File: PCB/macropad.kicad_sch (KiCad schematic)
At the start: 39 parts, among them SW1 SW_Push, SW10 SW_Push, SW11 SW_Push, SW12 SW_Push, SW13 SW_Push, SW14 SW_Push, SW15 SW_Push, SW16 SW_Push, SW2 SW_Push, SW3 SW_Push, SW4 SW_Push, SW5 SW_Push, SW6 SW_Push, SW7 SW_Push, SW8 SW_Push, SW9 SW_Push, U2 MOUDLE-SEEEDUINO-XIAO

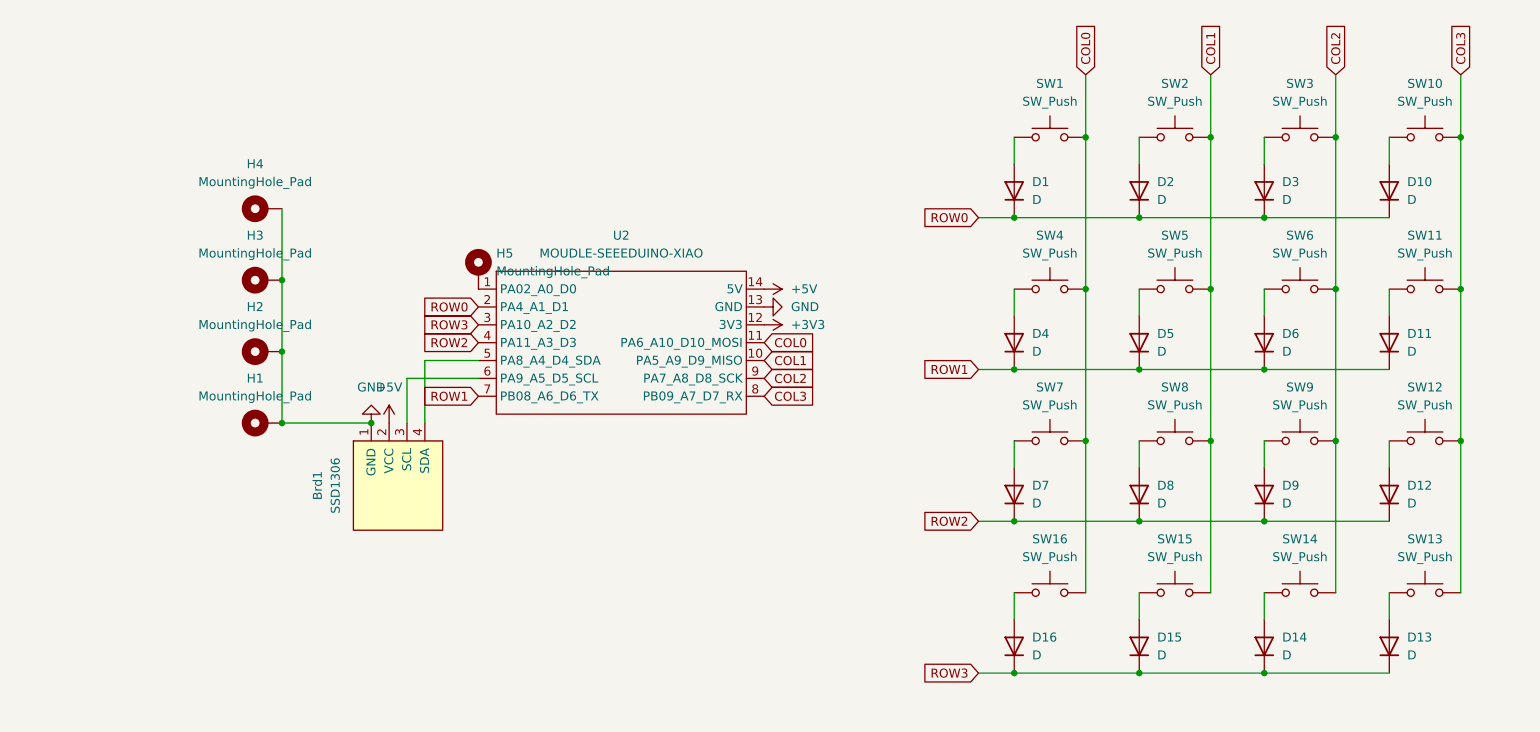
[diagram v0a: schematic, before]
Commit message: Add pullup resistors for I2C
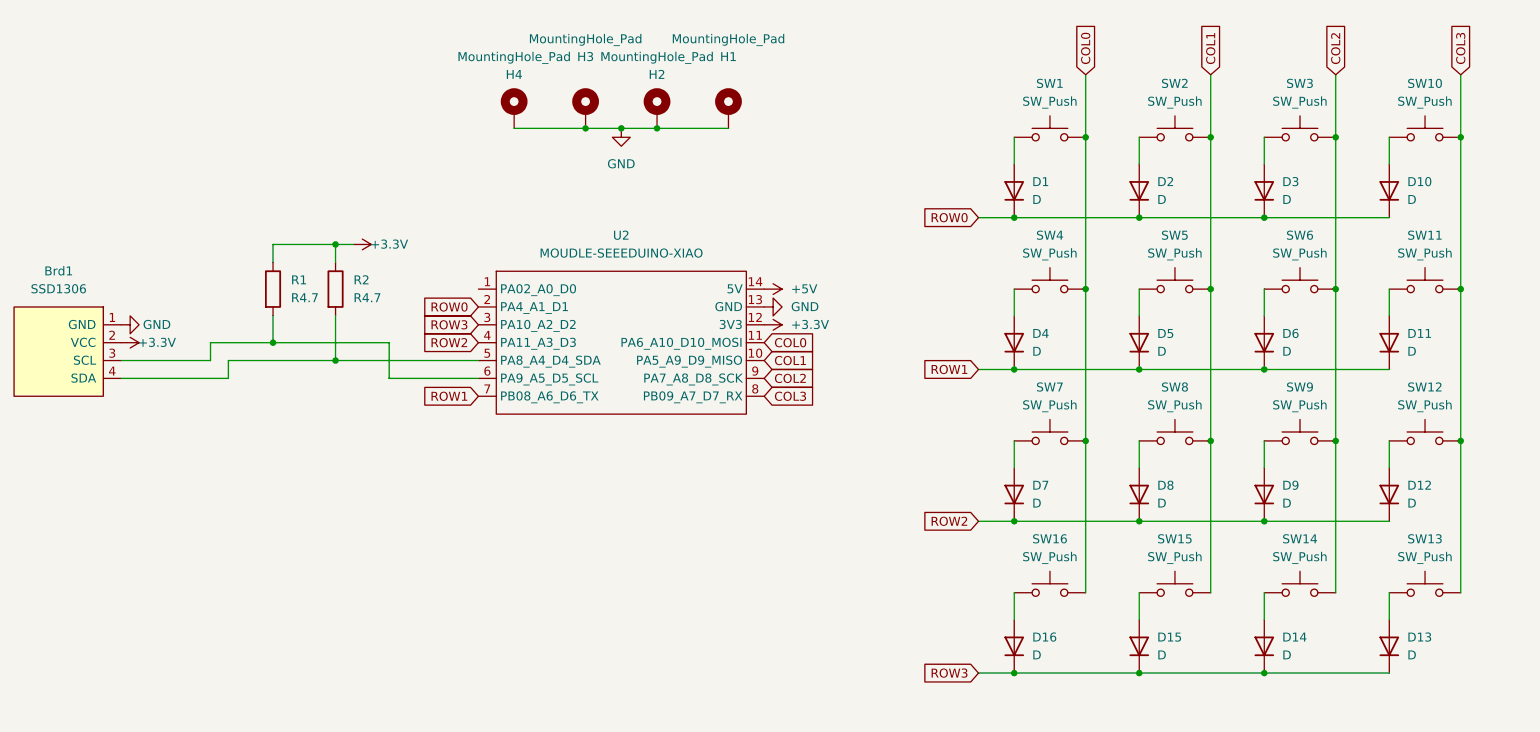
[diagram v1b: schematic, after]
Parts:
- removed H5: MountingHole_Pad, Connector_Wire:SolderWire-0.1sqmm_1x01_D0.4mm_OD1mm, symbol Mechanical:MountingHole_Pad
- added R1, R2: R4.7, Resistor_THT:R_Axial_DIN0204_L3.6mm_D1.6mm_P7.62mm_Horizontal, symbol Device:R
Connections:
- net +5V: no longer Brd1.2 (VCC)
- net at Brd1.4 (SDA), U2.5 (PA8_A4_D4_SDA): now also R2.2
- net at Brd1.3 (SCL), U2.6 (PA9_A5_D5_SCL): now also R1.2
- net +3V3 renamed +3.3V
- net +3.3V: now also Brd1.2 (VCC), R1.1, R2.1
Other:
- moved on the sheet: Brd1, H1, H2, H3, H4

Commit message: Misc improvements
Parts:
- D1, D10, D11, D12, D13, D14, D15, D16, D2, D3, D4, D5, D6, D7, D8, D9: value D -> Didode 1N4148
- H1, H2, H3, H4: value MountingHole_Pad -> Mounting Hole
- R1, R2: value R4.7 -> Resistor 4.7k ohm
- SW1, SW10, SW11, SW12, SW13, SW14, SW15, SW16, SW2, SW3, SW4, SW5, SW6, SW7, SW8, SW9: value SW_Push -> Kailh Choc V2
- U2: value MOUDLE-SEEEDUINO-XIAO -> SEEEDUINO XIAO RP2040
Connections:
- no-connect marks 0 -> 1
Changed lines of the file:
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@@
   (junction (at 176.53 132.08) (diameter 0) (color 0 0 0 0)
   )
+  (no_connect (at 82.55 77.47))
   (wire (pts (xy 176.53 110.49) (xy 194.31 110.49))
     (stroke (width 0) (type default))
@@
       (effects (font (size 1.27 1.27)) (justify right))
     )
-    (property "Value" "D" (at 196.85 129.54 90)
+    (property "Value" "Didode 1N4148" (at 196.85 129.54 90)
       (effects (font (size 1.27 1.27)) (justify right))
     )
@@
       (effects (font (size 1.27 1.27)) (justify right))
     )
-    (property "Value" "D" (at 214.63 64.77 90)
+    (property "Value" "Didode 1N4148" (at 214.63 64.77 90)
       (effects (font (size 1.27 1.27)) (justify right))
     )
@@
       (effects (font (size 1.27 1.27)) (justify right))
     )
-    (property "Value" "D" (at 161.29 107.95 90)
+    (property "Value" "Didode 1N4148" (at 161.29 107.95 90)
       (effects (font (size 1.27 1.27)) (justify right))
     )
@@
       (effects (font (size 1.27 1.27)) (justify right))
     )
-    (property "Value" "D" (at 196.85 107.95 90)
+    (property "Value" "Didode 1N4148" (at 196.85 107.95 90)
       (effects (font (size 1.27 1.27)) (justify right))
     )
@@
       (effects (font (size 1.27 1.27)))
     )
-    (property "Value" "MountingHole_Pad" (at 87.63 44.45 0)
+    (property "Value" "Mounting Hole" (at 87.63 44.45 0)
       (effects (font (size 1.27 1.27)))
     )
@@
       (effects (font (size 1.27 1.27)) (justify right))
     )
-    (property "Value" "D" (at 161.29 86.36 90)
+    (property "Value" "Didode 1N4148" (at 161.29 86.36 90)
       (effects (font (size 1.27 1.27)) (justify right))
     )
@@
       (effects (font (size 1.27 1.27)) (justify right))
     )
-    (property "Value" "D" (at 214.63 86.36 90)
+    (property "Value" "Didode 1N4148" (at 214.63 86.36 90)
       (effects (font (size 1.27 1.27)) (justify right))
     )
@@
       (effects (font (size 1.27 1.27)) (justify right))
     )
-    (property "Value" "D" (at 179.07 107.95 90)
+    (property "Value" "Didode 1N4148" (at 179.07 107.95 90)
       (effects (font (size 1.27 1.27)) (justify right))
     )
@@
       (effects (font (size 1.27 1.27)))
     )
-    (property "Value" "SW_Push" (at 181.61 72.39 0)
+    (property "Value" "Kailh Choc V2" (at 181.61 72.39 0)
       (effects (font (size 1.27 1.27)))
     )
@@
       (effects (font (size 1.27 1.27)))
     )
-    (property "Value" "SW_Push" (at 217.17 72.39 0)
+    (property "Value" "Kailh Choc V2" (at 217.17 72.39 0)
       (effects (font (size 1.27 1.27)))
     )
@@
       (effects (font (size 1.27 1.27)) (justify right))
     )
-    (property "Value" "D" (at 161.29 129.54 90)
+    (property "Value" "Didode 1N4148" (at 161.29 129.54 90)
       (effects (font (size 1.27 1.27)) (justify right))
     )
@@
       (effects (font (size 1.27 1.27)) (justify left))
     )
-    (property "Value" "R4.7" (at 55.88 78.74 0)
+    (property "Value" "Resistor 4.7k ohm" (at 55.88 78.74 0)
       (effects (font (size 1.27 1.27)) (justify left))
     )
@@
       (effects (font (size 1.27 1.27)))
     )
-    (property "Value" "SW_Push" (at 181.61 93.98 0)
+    (property "Value" "Kailh Choc V2" (at 181.61 93.98 0)
       (effects (font (size 1.27 1.27)))
     )
@@
       (effects (font (size 1.27 1.27)))
     )
-    (property "Value" "SW_Push" (at 217.17 115.57 0)
+    (property "Value" "Kailh Choc V2" (at 217.17 115.57 0)
       (effects (font (size 1.27 1.27)))
     )
@@
       (effects (font (size 1.27 1.27)) (justify right))
     )
-    (property "Value" "D" (at 161.29 64.77 90)
+    (property "Value" "Didode 1N4148" (at 161.29 64.77 90)
       (effects (font (size 1.27 1.27)) (justify right))
     )
@@
       (effects (font (size 1.27 1.27)))
     )
-    (property "Value" "MountingHole_Pad" (at 107.95 44.45 0)
+    (property "Value" "Mounting Hole" (at 107.95 44.45 0)
       (effects (font (size 1.27 1.27)))
     )
@@
       (effects (font (size 1.27 1.27)) (justify right))
     )
-    (property "Value" "D" (at 179.07 129.54 90)
+    (property "Value" "Didode 1N4148" (at 179.07 129.54 90)
       (effects (font (size 1.27 1.27)) (justify right))
     )
@@
       (effects (font (size 1.27 1.27)))
     )
-    (property "Value" "SW_Push" (at 217.17 93.98 0)
+    (property "Value" "Kailh Choc V2" (at 217.17 93.98 0)
       (effects (font (size 1.27 1.27)))
     )
@@
       (effects (font (size 1.27 1.27)) (justify right))
     )
-    (property "Value" "D" (at 214.63 107.95 90)
+    (property "Value" "Didode 1N4148" (at 214.63 107.95 90)
       (effects (font (size 1.27 1.27)) (justify right))
     )
@@
       (effects (font (size 1.27 1.27)))
     )
-    (property "Value" "SW_Push" (at 163.83 93.98 0)
+    (property "Value" "Kailh Choc V2" (at 163.83 93.98 0)
       (effects (font (size 1.27 1.27)))
     )
@@
       (effects (font (size 1.27 1.27)))
     )
-    (property "Value" "SW_Push" (at 199.39 50.8 0)
+    (property "Value" "Kailh Choc V2" (at 199.39 50.8 0)
       (effects (font (size 1.27 1.27)))
     )
@@
       (effects (font (size 1.27 1.27)))
     )
-    (property "Value" "SW_Push" (at 163.83 72.39 0)
+    (property "Value" "Kailh Choc V2" (at 163.83 72.39 0)
       (effects (font (size 1.27 1.27)))
     )
@@
       (effects (font (size 1.27 1.27)) (justify right))
     )
-    (property "Value" "D" (at 179.07 86.36 90)
+    (property "Value" "Didode 1N4148" (at 179.07 86.36 90)
       (effects (font (size 1.27 1.27)) (justify right))
     )
@@
       (effects (font (size 1.27 1.27)))
     )
-    (property "Value" "SW_Push" (at 181.61 115.57 0)
+    (property "Value" "Kailh Choc V2" (at 181.61 115.57 0)
       (effects (font (size 1.27 1.27)))
     )
@@
       (effects (font (size 1.27 1.27)) (justify right))
     )
-    (property "Value" "D" (at 214.63 129.54 90)
+    (property "Value" "Didode 1N4148" (at 214.63 129.54 90)
       (effects (font (size 1.27 1.27)) (justify right))
     )
@@
       (effects (font (size 1.27 1.27)))
     )
-    (property "Value" "SW_Push" (at 199.39 115.57 0)
+    (property "Value" "Kailh Choc V2" (at 199.39 115.57 0)
       (effects (font (size 1.27 1.27)))
     )
@@
       (effects (font (size 1.27 1.27)) (justify right))
     )
-    (property "Value" "D" (at 179.07 64.77 90)
+    (property "Value" "Didode 1N4148" (at 179.07 64.77 90)
       (effects (font (size 1.27 1.27)) (justify right))
     )
@@
       (effects (font (size 1.27 1.27)))
     )
-    (property "Value" "SW_Push" (at 181.61 50.8 0)
+    (property "Value" "Kailh Choc V2" (at 181.61 50.8 0)
       (effects (font (size 1.27 1.27)))
     )
@@
     )
   )
-  (symbol (lib_id "power:+3.3V") (at 64.77 71.12 270) (unit 1)
+  (symbol (lib_id "power:+3.3V") (at 64.77 71.12 0) (unit 1)
     (in_bom yes) (on_board yes) (dnp no)
-    (property "Reference" "#PWR06" (at 60.96 71.12 0)
-      (effects (font (size 1.27 1.27)) hide)
-    )
-    (property "Value" "+3.3V" (at 69.85 71.12 90)
+    (property "Reference" "#PWR06" (at 64.77 74.93 0)
+      (effects (font (size 1.27 1.27)) hide)
+    )
+    (property "Value" "+3.3V" (at 64.77 66.04 0)
       (effects (font (size 1.27 1.27)))
     )
@@
       (effects (font (size 1.27 1.27)))
     )
-    (property "Value" "SW_Push" (at 199.39 72.39 0)
+    (property "Value" "Kailh Choc V2" (at 199.39 72.39 0)
       (effects (font (size 1.27 1.27)))
     )
@@
       (effects (font (size 1.27 1.27)) (justify right))
     )
-    (property "Value" "D" (at 196.85 64.77 90)
+    (property "Value" "Didode 1N4148" (at 196.85 64.77 90)
       (effects (font (size 1.27 1.27)) (justify right))
     )
@@
       (effects (font (size 1.27 1.27)))
     )
-    (property "Value" "MOUDLE-SEEEDUINO-XIAO" (at 102.87 72.39 0)
+    (property "Value" "SEEEDUINO XIAO RP2040" (at 102.87 72.39 0)
       (effects (font (size 1.27 1.27)))
     )
@@
       (effects (font (size 1.27 1.27)))
     )
-    (property "Value" "SW_Push" (at 199.39 93.98 0)
+    (property "Value" "Kailh Choc V2" (at 199.39 93.98 0)
       (effects (font (size 1.27 1.27)))
     )
@@
       (effects (font (size 1.27 1.27)) (justify left))
     )
-    (property "Value" "R4.7" (at 64.77 78.74 0)
+    (property "Value" "Resistor 4.7k ohm" (at 64.77 78.74 0)
       (effects (font (size 1.27 1.27)) (justify left))
     )
@@
       (effects (font (size 1.27 1.27)) (justify right))
     )
-    (property "Value" "D" (at 196.85 86.36 90)
+    (property "Value" "Didode 1N4148" (at 196.85 86.36 90)
       (effects (font (size 1.27 1.27)) (justify right))
     )
@@
       (effects (font (size 1.27 1.27)))
     )
-    (property "Value" "SW_Push" (at 217.17 50.8 0)
+    (property "Value" "Kailh Choc V2" (at 217.17 50.8 0)
       (effects (font (size 1.27 1.27)))
     )
@@
       (effects (font (size 1.27 1.27)))
     )
-    (property "Value" "SW_Push" (at 163.83 115.57 0)
+    (property "Value" "Kailh Choc V2" (at 163.83 115.57 0)
       (effects (font (size 1.27 1.27)))
     )
@@
       (effects (font (size 1.27 1.27)))
     )
-    (property "Value" "SW_Push" (at 163.83 50.8 0)
+    (property "Value" "Kailh Choc V2" (at 163.83 50.8 0)
       (effects (font (size 1.27 1.27)))
     )
@@
       (effects (font (size 1.27 1.27)))
     )
-    (property "Value" "MountingHole_Pad" (at 97.79 41.91 0)
+    (property "Value" "Mounting Hole" (at 97.79 41.91 0)
       (effects (font (size 1.27 1.27)))
     )
@@
       (effects (font (size 1.27 1.27)))
     )
-    (property "Value" "MountingHole_Pad" (at 118.11 41.91 0)
-      (effects (font (size 1.27 1.27)))
-    )
+    (property "Value" "Mounting Hole" (at 118.11 41.91 0)
+      (effects (font (size 1.27 1.27)))
+    )

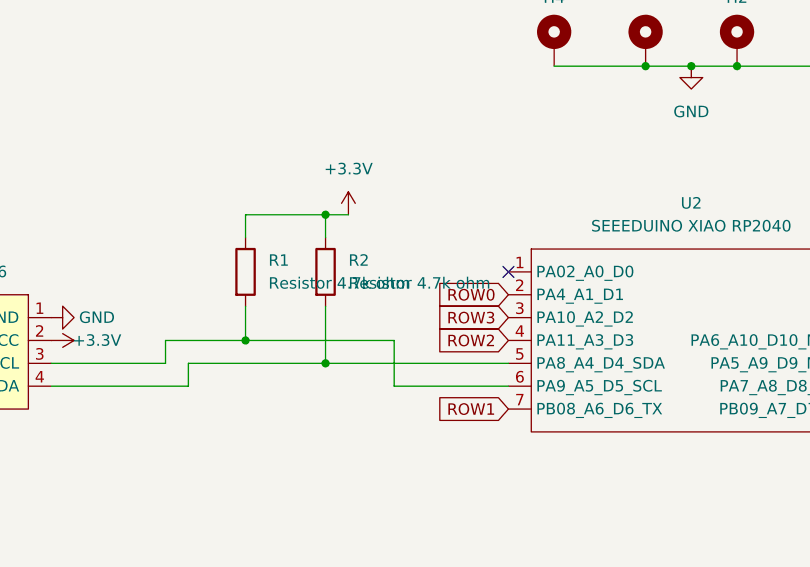
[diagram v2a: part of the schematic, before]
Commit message: Use thru-hole xiao
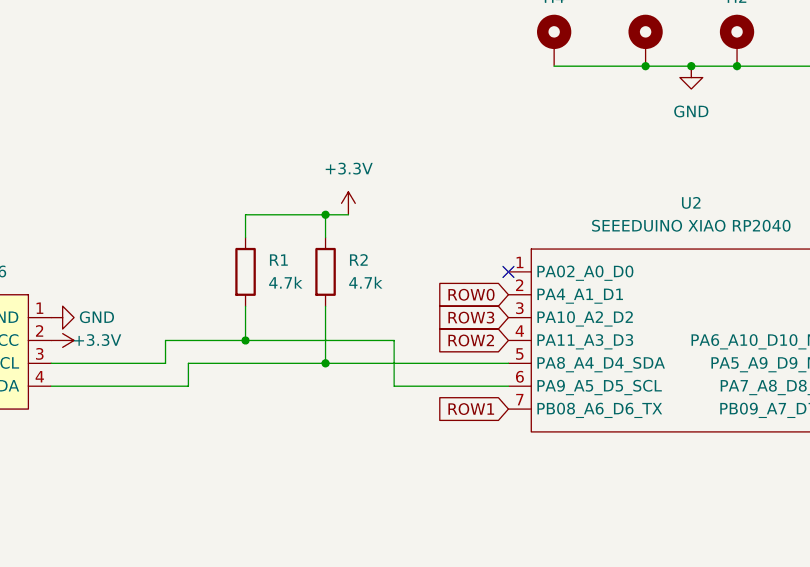
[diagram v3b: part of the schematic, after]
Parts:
- R1, R2: value Resistor 4.7k ohm -> 4.7k
- U2: footprint seed:XIAO-SAMD21-RP2040-14P-2.54-21X17.8MM (Seeeduino XIAO) -> seed:XIAO-Generic-Thruhole-14P-2.54-21X17.8MM
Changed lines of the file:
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@@
     (title "Cyao macropad")
     (date "2024-09-22")
-    (rev "v2.3")
+    (rev "v3.0")
     (company "Cheyao")
     (comment 1 "https://github.com/cheyao/macropad")
@@
   )
   (symbol (lib_id "Device:R") (at 53.34 77.47 0) (unit 1)
-    (in_bom yes) (on_board yes) (dnp no) (fields_autoplaced)
+    (in_bom yes) (on_board yes) (dnp no)
     (property "Reference" "R1" (at 55.88 76.2 0)
       (effects (font (size 1.27 1.27)) (justify left))
     )
-    (property "Value" "Resistor 4.7k ohm" (at 55.88 78.74 0)
+    (property "Value" "4.7k" (at 55.88 78.74 0)
       (effects (font (size 1.27 1.27)) (justify left))
     )
@@
       (effects (font (size 1.27 1.27)))
     )
-    (property "Footprint" "seed:XIAO-SAMD21-RP2040-14P-2.54-21X17.8MM (Seeeduino XIAO)" (at 85.09 82.55 0)
+    (property "Footprint" "seed:XIAO-Generic-Thruhole-14P-2.54-21X17.8MM" (at 85.09 82.55 0)
       (effects (font (size 1.27 1.27)) hide)
     )
@@
       (effects (font (size 1.27 1.27)) (justify left))
     )
-    (property "Value" "Resistor 4.7k ohm" (at 64.77 78.74 0)
+    (property "Value" "4.7k" (at 64.77 78.74 0)
       (effects (font (size 1.27 1.27)) (justify left))
     )

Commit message: Redisigned PCB
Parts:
- removed H1, H2, H3, H4: Mounting Hole, MountingHole:MountingHole_3.2mm_M3_Pad, symbol Mechanical:MountingHole_Pad
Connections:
- net COL0: now also U2.10 (PA5_A9_D9_MISO); no longer U2.11 (PA6_A10_D10_MOSI)
- net COL1: now also U2.9 (PA7_A8_D8_SCK); no longer U2.10 (PA5_A9_D9_MISO)
- net COL2: now also U2.8 (PB09_A7_D7_RX); no longer U2.9 (PA7_A8_D8_SCK)
- net COL3: now also U2.11 (PA6_A10_D10_MOSI); no longer U2.8 (PB09_A7_D7_RX)
- net ROW0: now also U2.7 (PB08_A6_D6_TX); no longer U2.2 (PA4_A1_D1)
- net ROW1: now also U2.4 (PA11_A3_D3); no longer U2.7 (PB08_A6_D6_TX)
- net ROW2: now also U2.3 (PA10_A2_D2); no longer U2.4 (PA11_A3_D3)
- net ROW3: now also U2.2 (PA4_A1_D1); no longer U2.3 (PA10_A2_D2)
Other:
- moved on the sheet: Brd1, R1, R2, U2
